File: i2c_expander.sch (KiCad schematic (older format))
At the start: 2 parts, among them U1 MCP23017_SO

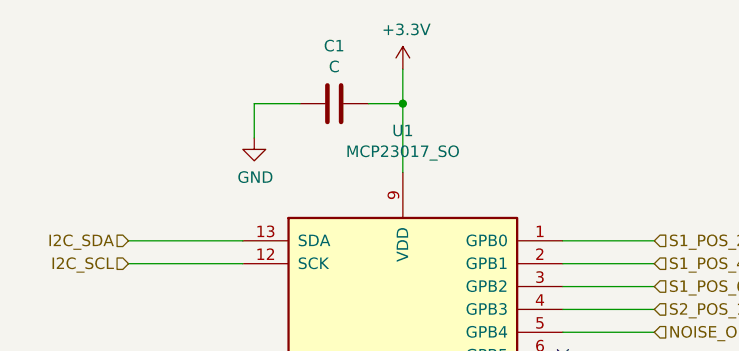
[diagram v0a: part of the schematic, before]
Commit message: Added MFN, MPN, VN and VPN fields for all symbols
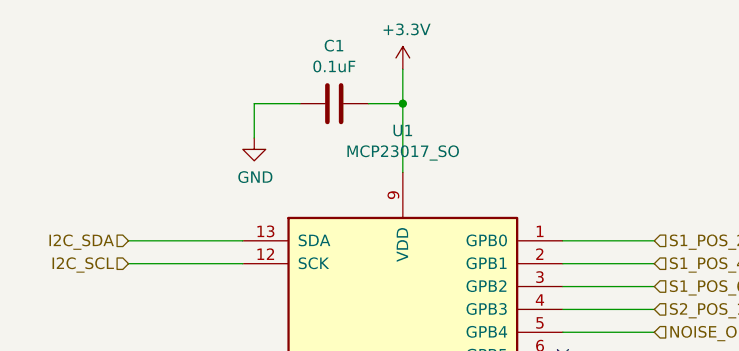
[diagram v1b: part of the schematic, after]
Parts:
- C1: value C -> 0.1uF; MFN (none) -> Generic; MPN (none) -> Generic; VN (none) -> Digikey; VPN (none) -> 311-1777-1-ND
- U1: MFN (none) -> Microchip Technology; MPN (none) -> MCP23017T-E/SO; VN (none) -> Digikey; VPN (none) -> MCP23017T-E/SOCT-ND
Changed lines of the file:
@@
 P 5550 2600
 F 0 "C1" V 5298 2600 50  0000 C CNN
-F 1 "C" V 5389 2600 50  0000 C CNN
+F 1 "0.1uF" V 5389 2600 50  0000 C CNN
 F 2 "Capacitor_SMD:C_0603_1608Metric_Pad1.05x0.95mm_HandSolder" H 5588 2450 50  0001 C CNN
 F 3 "~" H 5550 2600 50  0001 C CNN
+F 4 "Digikey" H 5550 2600 50  0001 C CNN "VN"
+F 5 "Generic" H 5550 2600 50  0001 C CNN "MFN"
+F 6 "Generic" H 5550 2600 50  0001 C CNN "MPN"
+F 7 "311-1777-1-ND" H 5550 2600 50  0001 C CNN "VPN"
 	1    5550 2600
 	0    1    1    0
@@
 F 2 "Package_SO:SOIC-28W_7.5x17.9mm_P1.27mm" H 6050 3000 50  0001 L CNN
 F 3 "http://ww1.microchip.com/downloads/en/DeviceDoc/20001952C.pdf" H 6050 2900 50  0001 L CNN
+F 4 "Digikey" H 5850 4000 50  0001 C CNN "VN"
+F 5 "Microchip Technology" H 5850 4000 50  0001 C CNN "MFN"
+F 6 "MCP23017T-E/SO" H 5850 4000 50  0001 C CNN "MPN"
+F 7 "MCP23017T-E/SOCT-ND" H 5850 4000 50  0001 C CNN "VPN"
 	1    5850 4000
 	1    0    0    -1
